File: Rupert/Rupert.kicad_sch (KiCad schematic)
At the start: 26 parts, among them U1 Spark_Max#9

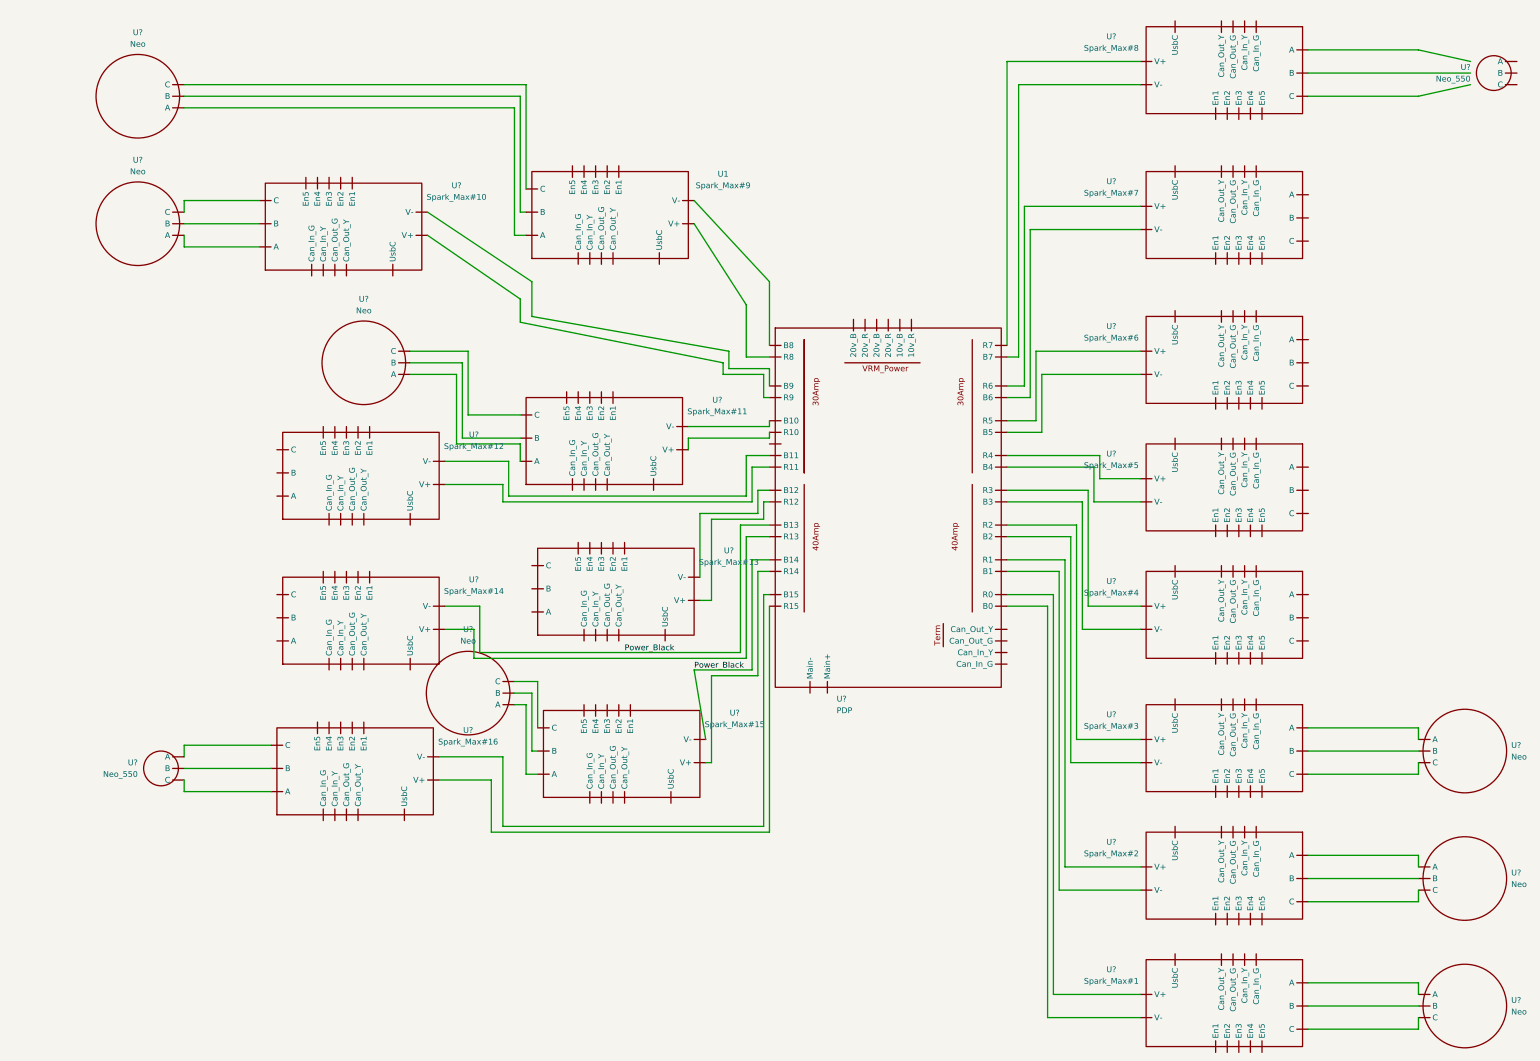
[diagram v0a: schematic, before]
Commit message: Moved some things around
Not really any change but moved to make more readable
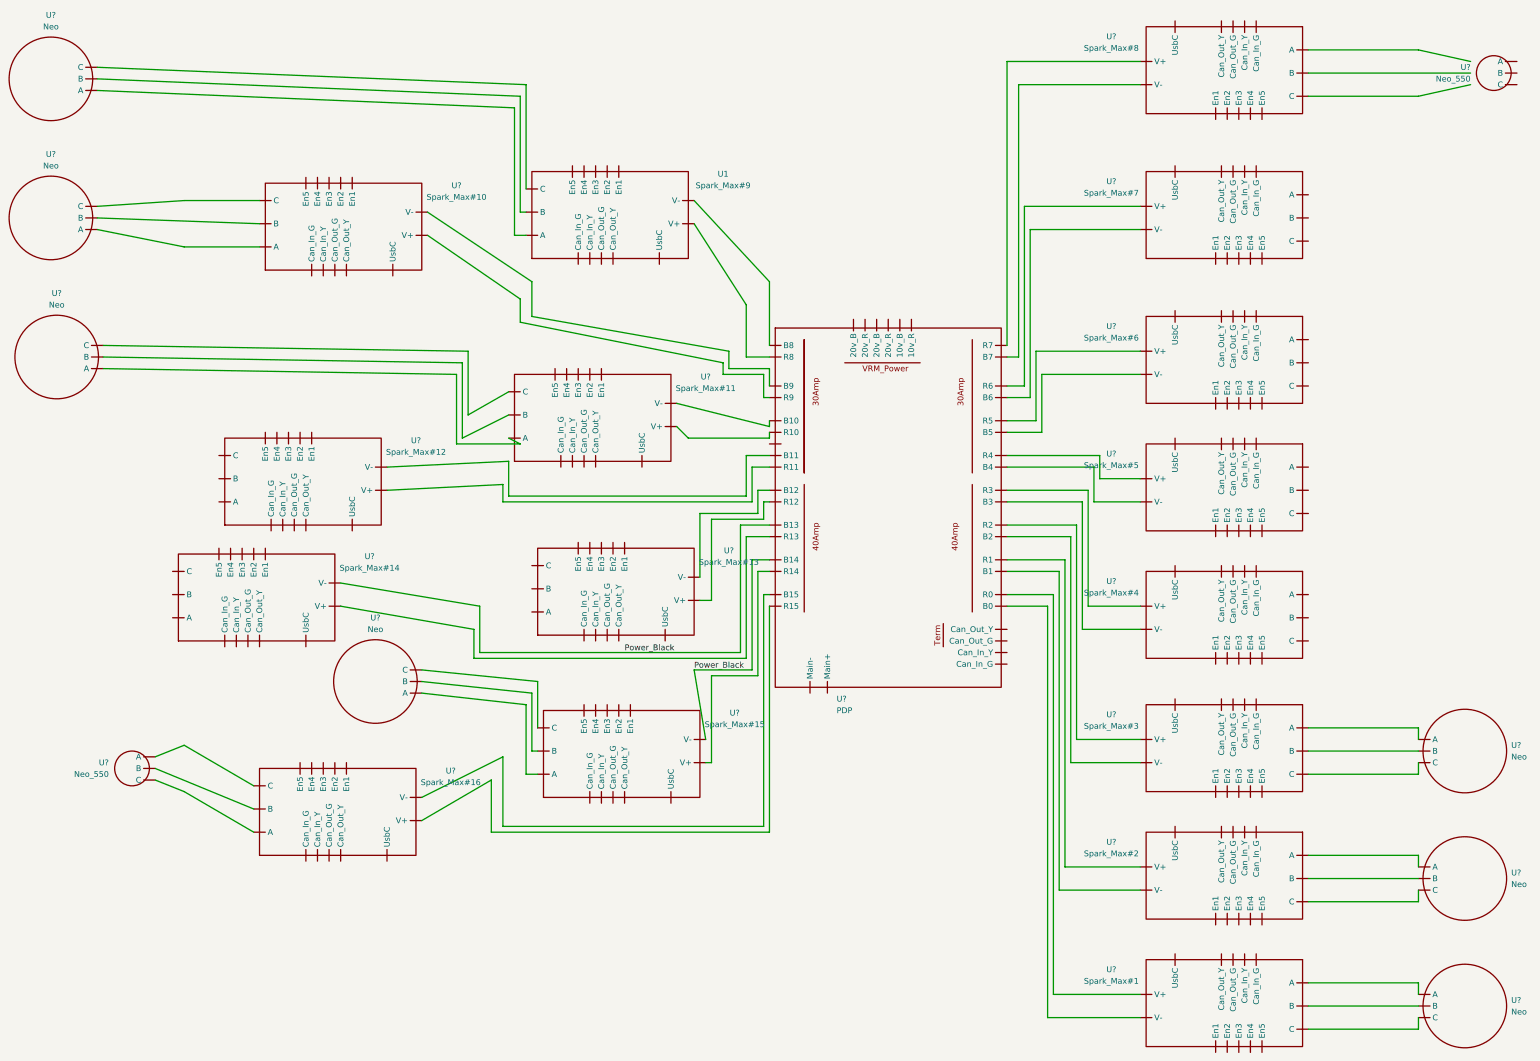
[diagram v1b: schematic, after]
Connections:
- net at U?. (V-): now also U?. (R9); no longer U?. (C)
- net at U?. (V-): no longer U?. (C) (x2)
- net at U?. (V-): now also U?. (R9) (x4)
- net at U?. (V-): now also U?. (C) (x2)
- net at U1. (V-): no longer U?. (C)
- net at U?. (V-): no longer U?. (R9) (x4)
- new net: U?. (R9), U?. (V-) (x23)
- new net: U?. (C), U?. (V-) (x14)
- new net: U1. (V-), U?. (C) (x2)
- new net: U1. (V-), U?. (R9) (x2)
- now unconnected: U1. (V-), U1. (V-), U1. (V-), U?. (V-), U?. (V-), U?. (V-), U?. (V-), U?. (V-), U?. (V-), U?. (V-), U?. (V-), U?. (V-), U?. (V-), U?. (V-), U?. (V-)
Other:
- moved on the sheet: U?
